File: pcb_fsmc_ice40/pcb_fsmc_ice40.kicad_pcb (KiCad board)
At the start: 2 copper layers, 76.2 x 32 mm, 44 parts, among them P2 CONN_01X20, P3 CONN_01X20, P4 MICRO-SD, P5 CONN_01X12, P6 CONN_01X12, P7 KNUSB, U1 STM32F40X_LQFP144, X1 CRYSTAL

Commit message: Mostly complete routing.
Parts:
- removed JP1: Jumper_NO_Small, Pin_Headers:Pin_Header_Straight_1x02
- removed P3: CONN_01X20, knielsenlib:ice40_vert_conn
- removed P4: MICRO-SD, knielsenlib:SD_502774
- removed P6: CONN_01X12, knielsenlib:ice40_top_conn_12
- added P1: SD_CARD, knielsenlib:SD_CARD_10100, B.Cu at (170.8, 111.7)
- added REF**: MountingHole_3.2mm_M3, Mounting_Holes:MountingHole_3.2mm_M3, F.Cu at (103.0, 87.0)
- added REF**: MountingHole_3.2mm_M3, Mounting_Holes:MountingHole_3.2mm_M3, F.Cu at (103.0, 113.0)
- added SW1: SWITCH_INV, knielsenlib:switch_msk_12c02, B.Cu at (123.0, 85.8)
- B1: footprint knielsenlib:SWITCH_FSMJSMA -> knielsenlib:pushbutton_EVQ_PSR02K
- C13, D1, D2, R1, R2: moved to F.Cu
- C30, R4: moved to B.Cu
- P2: value CONN_01X20 -> CONN_02X20; moved to F.Cu
- P5: value CONN_01X12 -> CONN_02X12
- moved R4 54.1 mm to (123.2, 91.0), turned to 180 degrees
- moved R5 37.7 mm to (126.6, 121.7), turned to 90 degrees
- moved R3 34.5 mm to (134.0, 94.8), turned to 0 degrees
- moved R1 33.8 mm to (167.4, 87.2), turned to 0 degrees
- moved D1 33.3 mm to (167.4, 85.5), turned to 180 degrees
- moved R2 32.9 mm to (164.2, 87.2), turned to 0 degrees
- moved D2 32.3 mm to (164.2, 85.5), turned to 180 degrees
- moved P7 24.4 mm to (174.5, 89.7)
- moved P5 21.0 mm to (145.7, 85.8), turned to 0 degrees
- moved C29 20.0 mm to (116.9, 87.1), turned to 90 degrees
- moved C30 19.1 mm to (144.8, 110.6)
- moved B1 18.7 mm to (113.9, 87.1), turned to 90 degrees
- moved L1 14.6 mm to (169.5, 94.2), turned to 90 degrees
- moved X1 10.1 mm to (113.5, 110.5)
- moved C20 9.92 mm to (117.1, 112.0)
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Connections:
- P2 pad 10: /sram_d10 -> /sram_we
- P2 pad 11: /sram_d8 -> /sram_d0
- P2 pad 12: GND -> /sram_d1
- P2 pad 13: /sram_d6 -> /sram_d14
- P2 pad 14: /sram_d4 -> /sram_d15
- P2 pad 15: /sram_a6 -> GND
- P2 pad 17: /sram_a1 -> /sram_d12
- P2 pad 18: /sram_a3 -> /sram_d13
- P2 pad 19: /sram_a5 -> /sram_d10
- P2 pad 2: /sram_d2 -> +3.3V
- P2 pad 20: GND -> /sram_d11
- P2 pad 3: /sram_oe -> /fpga_io1
- P2 pad 4: GND -> /sram_d2
- P2 pad 5: /sram2_ce -> /sram_oe
- P2 pad 6: /sram_d0 -> /sram_d3
- P2 pad 7: /sram_d14 -> GND
- P2 pad 9: /sram_d12 -> /sram2_ce
- P5 pad 1: Net-(P5-Pad1) -> GND
- P5 pad 10: Net-(P5-Pad10) -> /pb7
- P5 pad 11: Net-(P5-Pad11) -> /pb4
- P5 pad 12: Net-(P5-Pad12) -> /pb5
- P5 pad 2: Net-(P5-Pad2) -> GND
- P5 pad 3: Net-(P5-Pad3) -> +3.3V
- P5 pad 4: Net-(P5-Pad4) -> +3.3V
- P5 pad 5: Net-(P5-Pad5) -> /pe0
- P5 pad 6: Net-(P5-Pad6) -> /pe1
- P5 pad 7: Net-(P5-Pad7) -> /pb8
- P5 pad 8: Net-(P5-Pad8) -> /pb9
- P5 pad 9: Net-(P5-Pad9) -> /pb6
- R1 pad 1: +3.3V -> /user_led1
- R2 pad 1: /user_led -> /user_led2
- R4 pad 1: GND -> /boot0
- R4 pad 2: /boot0 -> GND
- U1 pad 100: /pa8 -> /user_led1
- U1 pad 101: /pa9 -> /user_led2
- U1 pad 110: /pa15 -> /sd_wp
- U1 pad 127: /sram4_ce -> /pg12
- U1 pad 132: /user_led -> /pg15
- U1 pad 133: /swo -> /pb3
- U1 pad 141: /sram_ble -> /pe0
- U1 pad 142: /sram_bhe -> /pe1
- U1 pad 7: /sd_cd -> /pc13
- U1 pad 73: /pb12 -> /fpga_io1
- U1 pad 74: /pb13 -> /fpga_io2
- U1 pad 8: /sd_wp -> /pc14
- U1 pad 91: /pg6 -> /sd_cd
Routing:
- net +3.3V: track 157.9 -> 250.6 mm, vias 0 -> 19
- net GND: track 0.00 -> 80.6 mm, vias 0 -> 30
- net /user_led1: track 0.00 -> 34.7 mm, vias 0 -> 2
- net /fpga_io2: track 0.00 -> 32.1 mm, vias 0 -> 1
- net /user_led2: track 0.00 -> 31.3 mm, vias 0 -> 2
- net /pg12: track 0.00 -> 30.8 mm
- net /fpga_io1: track 0.00 -> 29.5 mm, vias 0 -> 1
- net /pg13: track 0.00 -> 28.8 mm
- net /pg14: track 0.00 -> 26.8 mm
- net /pb3: track 0.00 -> 26.2 mm
- net /pb8: track 0.00 -> 25.2 mm, vias 0 -> 1
- net /pb9: track 0.00 -> 24.8 mm
- net /pb4: track 0.00 -> 24.7 mm, vias 0 -> 1
- net /pb5: track 0.00 -> 24.7 mm
- net /pb6: track 0.00 -> 23.6 mm, vias 0 -> 1
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- added copper zone on F.Cu, net +3.3V
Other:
- board size 76.2 x 32 mm -> 76.2 x 48 mm
- board text added: "1"
- board text added: "2"
- board text added: "39"
- board text added: "3V3"
- board text added: "40"
- board text added: "5V"
- board text added: "GND"
- board text added: "NRST"
- board text added: "PB3"
- board text added: "PB4"
- board text added: "PB5"
- board text added: "PB6"
- board text added: "PB7"
- board text added: "PB8"
- board text added: "PB9"
- board text added: "PE0"
- board text added: "PE1"
- board text added: "PG12"
- board text added: "PG13"
- board text added: "PG14"
- board text added: "SWCLK"
- board text added: "SWD"
- board text added: "SWDIO"

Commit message: Mostly complete routing now.
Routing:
- net /sram_d15: track 20.6 -> 41.0 mm
- net /sd_d3: track 39.1 -> 35.3 mm
- net /sd_cmd: track 39.8 -> 37.0 mm
- net /sd_d2: track 40.7 -> 38.0 mm
- net /nrst: track 73.1 -> 74.5 mm
- net /sram_d13: track 18.1 -> 17.1 mm
- net +3.3V: track 250.6 -> 249.6 mm
- net (no net): track 0.99 -> 0.00 mm
- net /sram_d7: track 12.9 -> 11.9 mm
- net /sram_a1: track 32.3 -> 31.6 mm
- net /sram_d14: track 19.7 -> 20.3 mm
- net /sd_clk: track 25.5 -> 25.0 mm
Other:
- board text added: "APP"
- board text added: "DFU"
- board text added: "RESET"

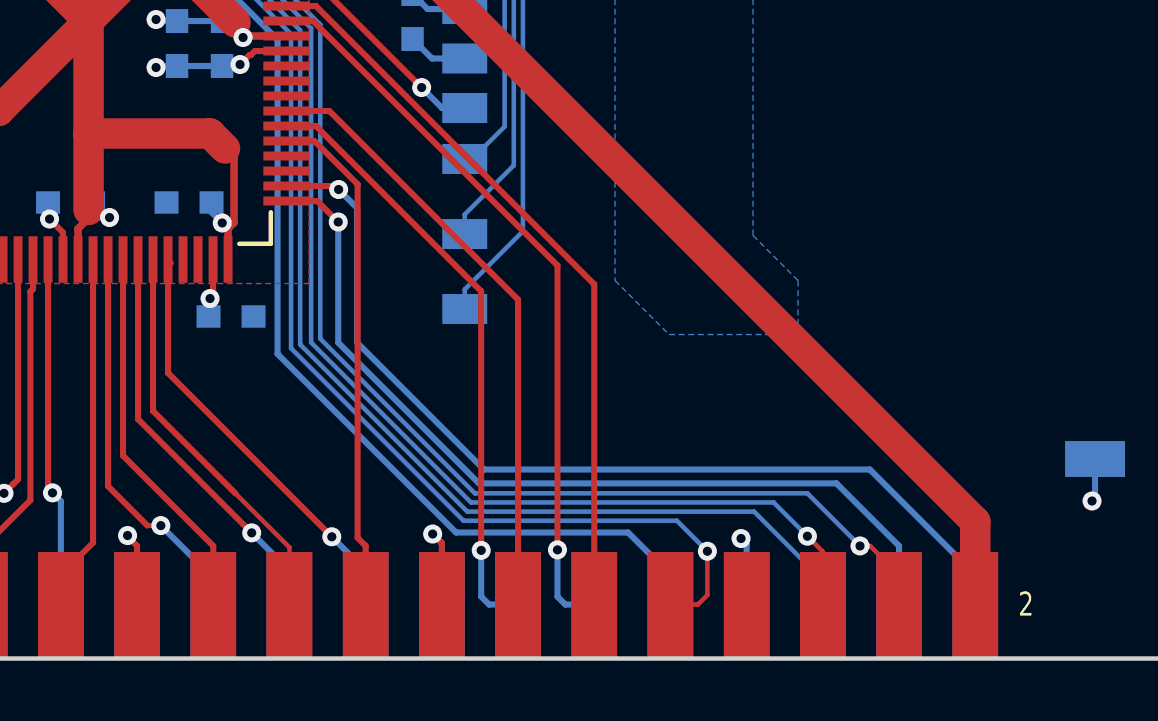
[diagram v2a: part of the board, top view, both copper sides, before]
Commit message: Move the extra IO fpga_io1 and fpga_io2 to PB10/PB11.
These have USART Rx/Tx available, so we can use these two spare IOs
with the trick wher ethe FPGA proxies the UART signal from STM32 to
the FTDI chip on the ICE40 board, simplifying serial debugging.
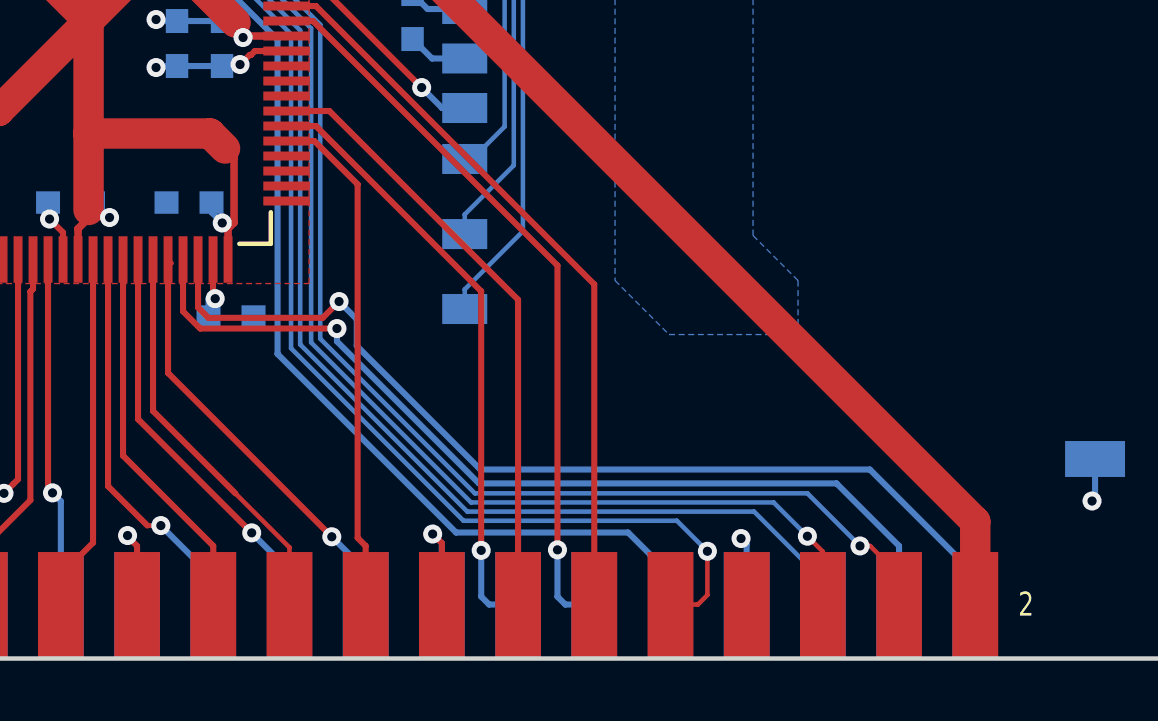
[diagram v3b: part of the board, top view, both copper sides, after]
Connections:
- U1 pad 69: /pb10 -> /fpga_io1
- U1 pad 70: /pb11 -> /fpga_io2
- U1 pad 73: /fpga_io1 -> /pb12
- U1 pad 74: /fpga_io2 -> /pb13
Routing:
- net /fpga_io1: track 29.5 -> 31.0 mm
- net /fpga_io2: track 31.9 -> 33.2 mm

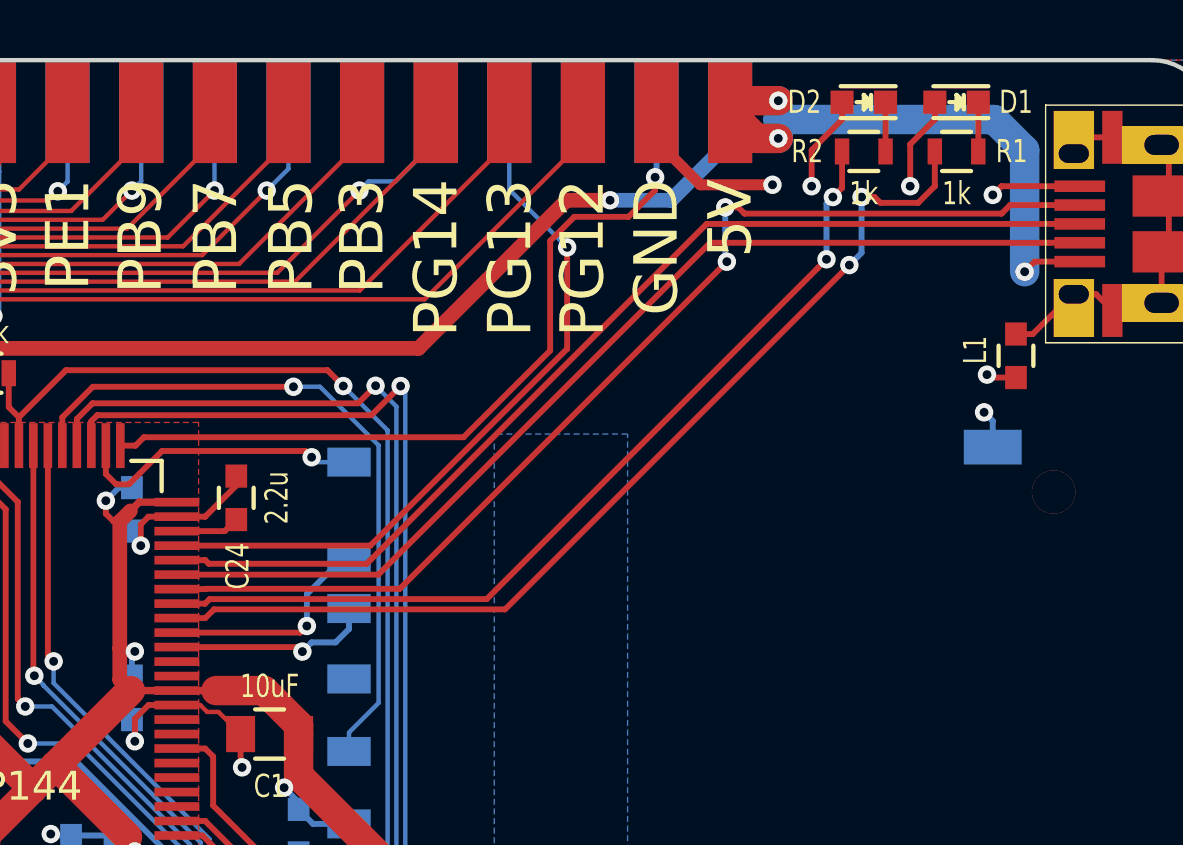
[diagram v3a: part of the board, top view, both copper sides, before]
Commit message: Connect PA9 to usb_5v, as used by some ST library code.
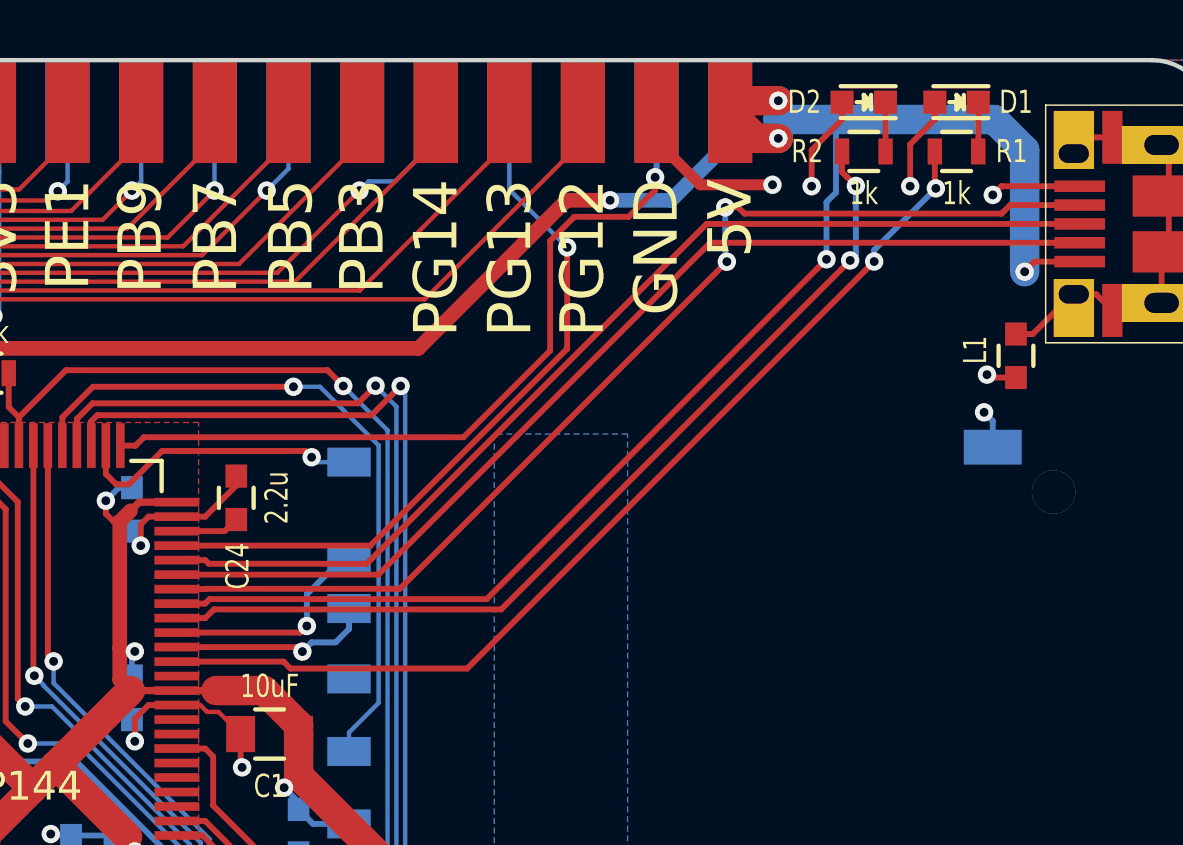
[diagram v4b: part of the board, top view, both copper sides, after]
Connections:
- U1 pad 100: /user_led1 -> /user_led2
- U1 pad 101: /user_led2 -> /usb_5v
- U1 pad 97: /pc7 -> /user_led1
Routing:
- net /usb_5v: track 20.3 -> 52.6 mm, vias 3 -> 4
- net /user_led2: track 31.3 -> 32.4 mm
